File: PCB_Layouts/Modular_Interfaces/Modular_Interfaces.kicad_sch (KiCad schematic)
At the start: 34 parts, among them J1 USB_A, J10 Conn_01x10_Socket, J11 Conn_01x04_Socket, J12 Conn_01x10_Socket, J2 Conn_01x10_Socket, J3 Conn_01x10_Socket, J4 Conn_01x10_Socket, J5 Conn_01x10_Socket, J6 RJ45_LED, J7 Conn_01x10_Socket, J8 Conn_01x03_Socket, J9 Conn_01x10_Socket, U1 ENC28J60x-SS, Y1 25MHz

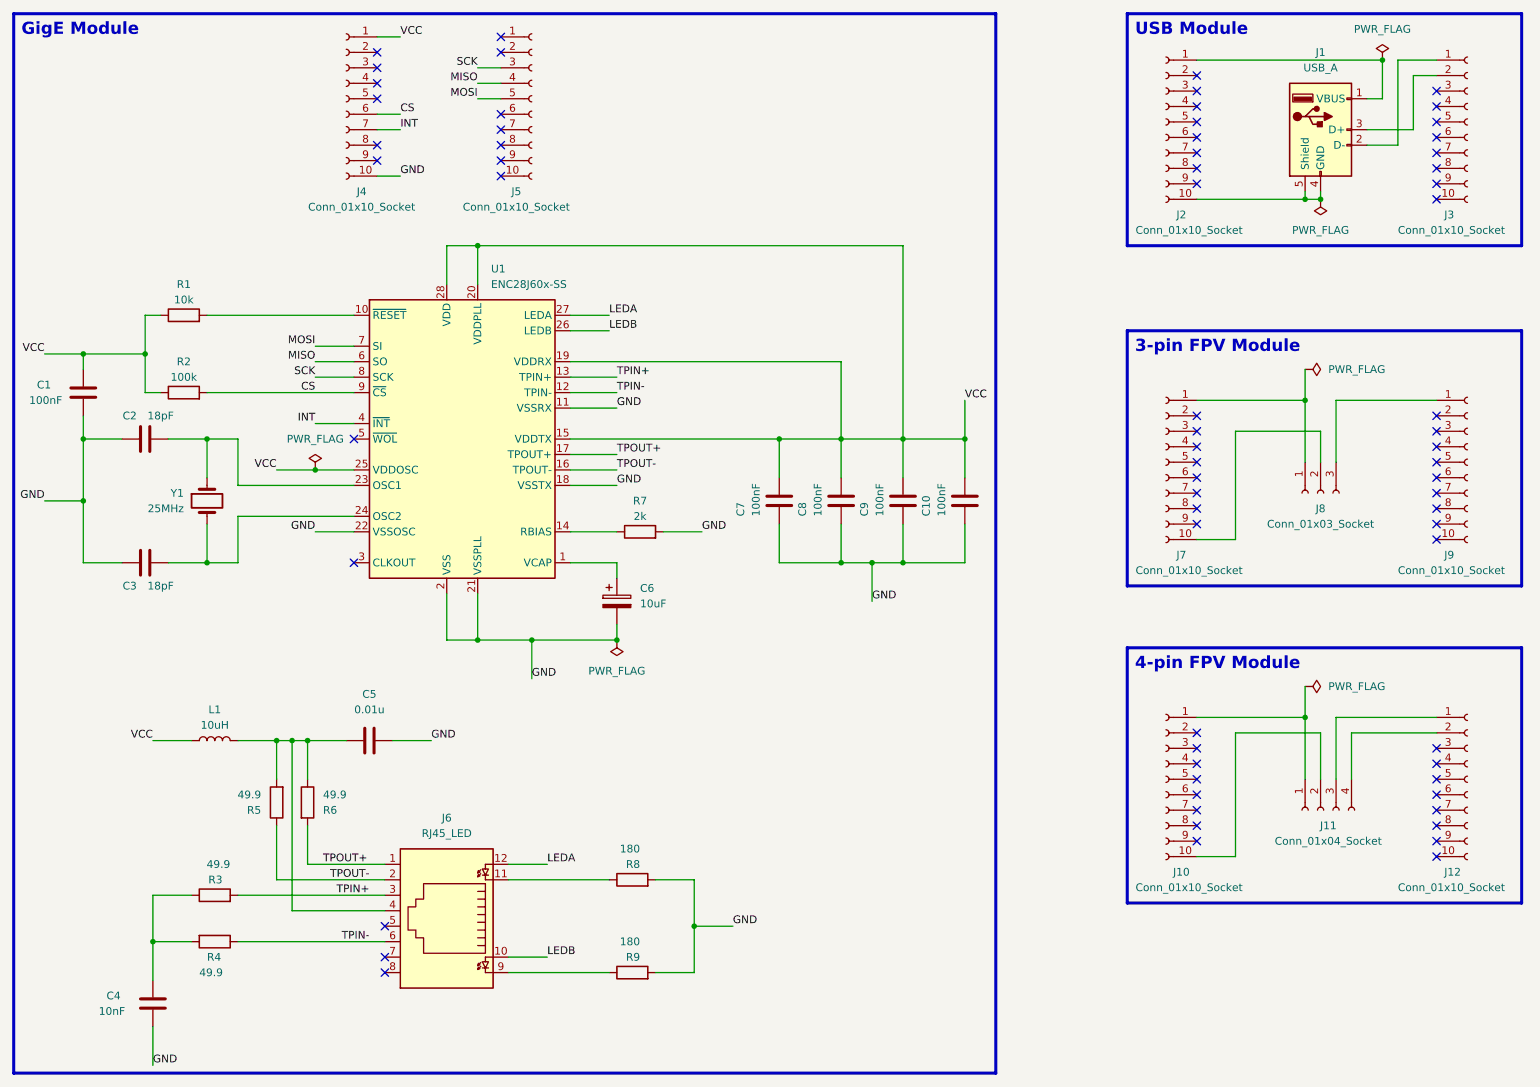
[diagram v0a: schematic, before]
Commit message: Updating modular interfaces module and quote
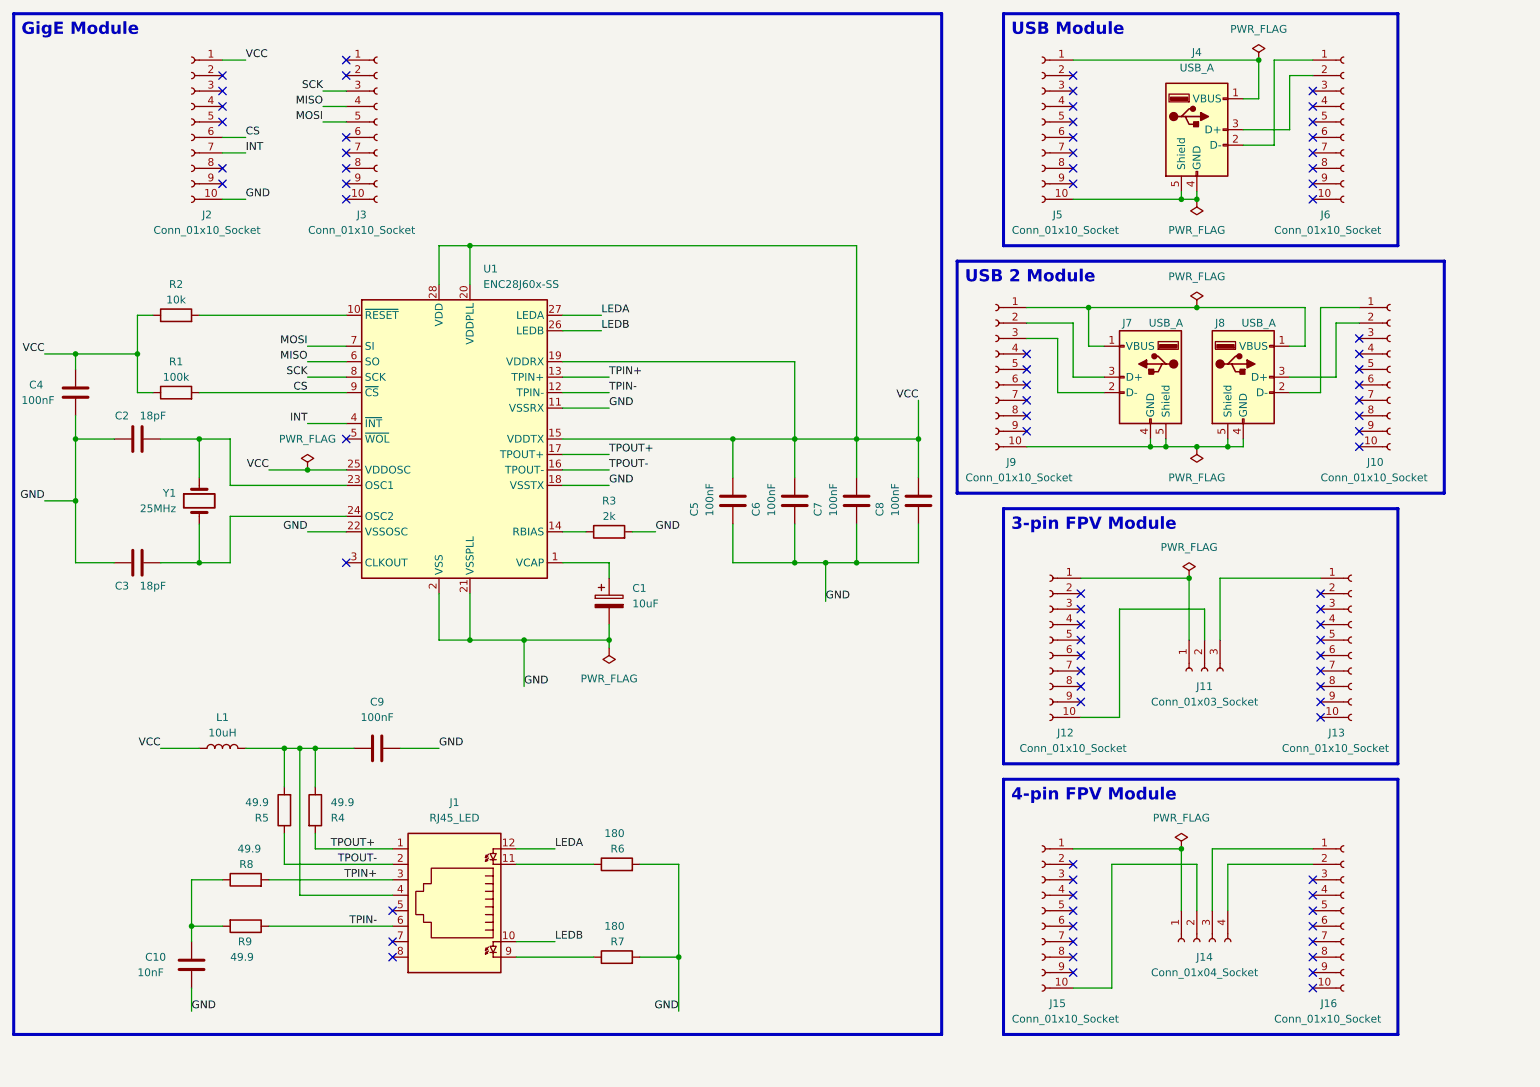
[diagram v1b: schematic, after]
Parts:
- removed C1: 100nF, Capacitor_Tantalum_SMD:CP_EIA-1608-08_AVX-J, symbol Device:C
- removed C6: 10uF, Capacitor_Tantalum_SMD:CP_EIA-1608-08_AVX-J, symbol Device:C_Polarized
- removed J1: USB_A, Connector_USB:USB_A_TE_292303-7_Horizontal, symbol Connector:USB_A
- removed J11: Conn_01x04_Socket, Connector_JST:JST_PH_B4B-PH-K_1x04_P2.00mm_Vertical, symbol Connector:Conn_01x04_Socket
- removed J4, J7: Conn_01x10_Socket, Connector_PinSocket_2.00mm:PinSocket_1x10_P2.00mm_Vertical, symbol Connector:Conn_01x10_Socket
- removed J6: RJ45_LED, Connector_RJ:RJ45_Amphenol_RJHSE538X, symbol Connector:RJ45_LED
- removed J8: Conn_01x03_Socket, Connector_JST:JST_PH_B3B-PH-K_1x03_P2.00mm_Vertical, symbol Connector:Conn_01x03_Socket
- added C1: 10uF, Capacitor_SMD:CP_Elec_4x5.4, symbol Device:C_Polarized
- added C6: 100nF, Capacitor_SMD:C_0603_1608Metric, symbol Device:C
- added J1: RJ45_LED, Connector_RJ:RJ45_Amphenol_RJHSE538X, symbol Connector:RJ45_LED
- added J11: Conn_01x03_Socket, Connector_JST:JST_XH_B3B-XH-A_1x03_P2.50mm_Vertical, symbol Connector:Conn_01x03_Socket
- added J13, J15, J16, J6: Conn_01x10_Socket, Connector_PinSocket_2.00mm:PinSocket_1x10_P2.00mm_Vertical, symbol Connector:Conn_01x10_Socket
- added J14: Conn_01x04_Socket, Connector_JST:JST_XH_B4B-XH-A_1x04_P2.50mm_Vertical, symbol Connector:Conn_01x04_Socket
- added J4, J7, J8: USB_A, Connector_USB:USB_A_Stewart_SS-52100-001_Horizontal, symbol Connector:USB_A
- C10: value 100nF -> 10nF; footprint Capacitor_Tantalum_SMD:CP_EIA-1608-08_AVX-J -> Capacitor_SMD:C_0603_1608Metric
- C2, C3, C7, C8, C9: footprint Capacitor_Tantalum_SMD:CP_EIA-1608-08_AVX-J -> Capacitor_SMD:C_0603_1608Metric
- C4: value 10nF -> 100nF; footprint Capacitor_Tantalum_SMD:CP_EIA-1608-08_AVX-J -> Capacitor_SMD:C_0603_1608Metric
- C5: value 0.01u -> 100nF; footprint Capacitor_Tantalum_SMD:CP_EIA-1608-08_AVX-J -> Capacitor_SMD:C_0603_1608Metric
- L1: footprint Inductor_SMD:L_0603_1608Metric -> Inductor_SMD:L_0201_0603Metric_Pad0.64x0.40mm_HandSolder
- R1: value 10k -> 100k
- R2: value 100k -> 10k
- R3: value 49.9 -> 2k
- R6: value 49.9 -> 180
- R7: value 2k -> 180
- R8, R9: value 180 -> 49.9
- Y1: footprint Crystal:Crystal_SMD_MicroCrystal_CC4V-T1A-2Pin_5.0x1.9mm -> Crystal:Crystal_SMD_MicroCrystal_CC8V-T1A-2Pin_2.0x1.2mm
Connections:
- net CS: now also J2.6 (Pin_6), R1.2; no longer R2.2
- net GND: now also J2.10 (Pin_10), R3.2, R6.2, C1.2, C6.2; no longer R8.2, R9.2
- net INT: now also J2.7 (Pin_7)
- net LEDA: now also J1.12
- net LEDB: now also J1.10
- net MISO: now also J3.4 (Pin_4); no longer J5.4 (Pin_4)
- net MOSI: now also J3.5 (Pin_5); no longer J5.5 (Pin_5)
- net SCK: now also J3.3 (Pin_3); no longer J5.3 (Pin_3)
- net TPIN+: now also R8.2, J1.3; no longer R3.2
- net TPIN-: now also R9.1, J1.6; no longer R4.1
- net TPOUT+: now also R4.2, J1.1; no longer R6.2
- net TPOUT-: now also J1.2
- net VCC: now also C4.1, C5.1, J2.1 (Pin_1), C6.1; no longer C10.1, C9.1
- net at J5.1 (Pin_1): now also J4.1 (VBUS)
- net at J5.10 (Pin_10): now also J4.4 (GND), J4.5 (Shield)
- net at L1.2, R5.2: now also C9.1, R4.1, J1.4; no longer C5.1, R6.1
- net at U1.1 (VCAP): now also C1.1
- net at J9.1 (Pin_1): now also J7.1 (VBUS), J8.1 (VBUS)
- net at R8.1: now also C10.1, R9.2
- net at J10.1 (Pin_1): now also J8.2 (D-)
- net at J10.2 (Pin_2): now also J8.3 (D+)
- net at J12.1 (Pin_1): now also J11.1 (Pin_1)
- net at J12.10 (Pin_10): now also J11.2 (Pin_2)
- net at U1.10 (~{RESET}): now also R2.2; no longer R1.2
- net at R7.1: now also J1.9; no longer U1.14 (RBIAS)
- net at J9.10 (Pin_10): now also J7.4 (GND), J7.5 (Shield), J8.4 (GND), J8.5 (Shield)
- net at J9.2 (Pin_2): now also J7.3 (D+)
- net at J9.3 (Pin_3): now also J7.2 (D-)
- new net: J14.1 (Pin_1), J15.1 (Pin_1)
- new net: J14.2 (Pin_2), J15.10 (Pin_10)
- new net: J1.11, R6.1
- new net: J4.2 (D-), J6.1 (Pin_1)
- new net: J4.3 (D+), J6.2 (Pin_2)
- new net: J11.3 (Pin_3), J13.1 (Pin_1)
- new net: R3.1, U1.14 (RBIAS)
- new net: J14.3 (Pin_3), J16.1 (Pin_1)
- new net: J14.4 (Pin_4), J16.2 (Pin_2)
- no-connect marks 67 -> 81
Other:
- note added: "USB 2 Module"
